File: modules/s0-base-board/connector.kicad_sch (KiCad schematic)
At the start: 6 parts, among them J5 Conn_02x23_Odd_Even, J6 Conn_02x23_Odd_Even, U6 BEAGLEBONEBLACK

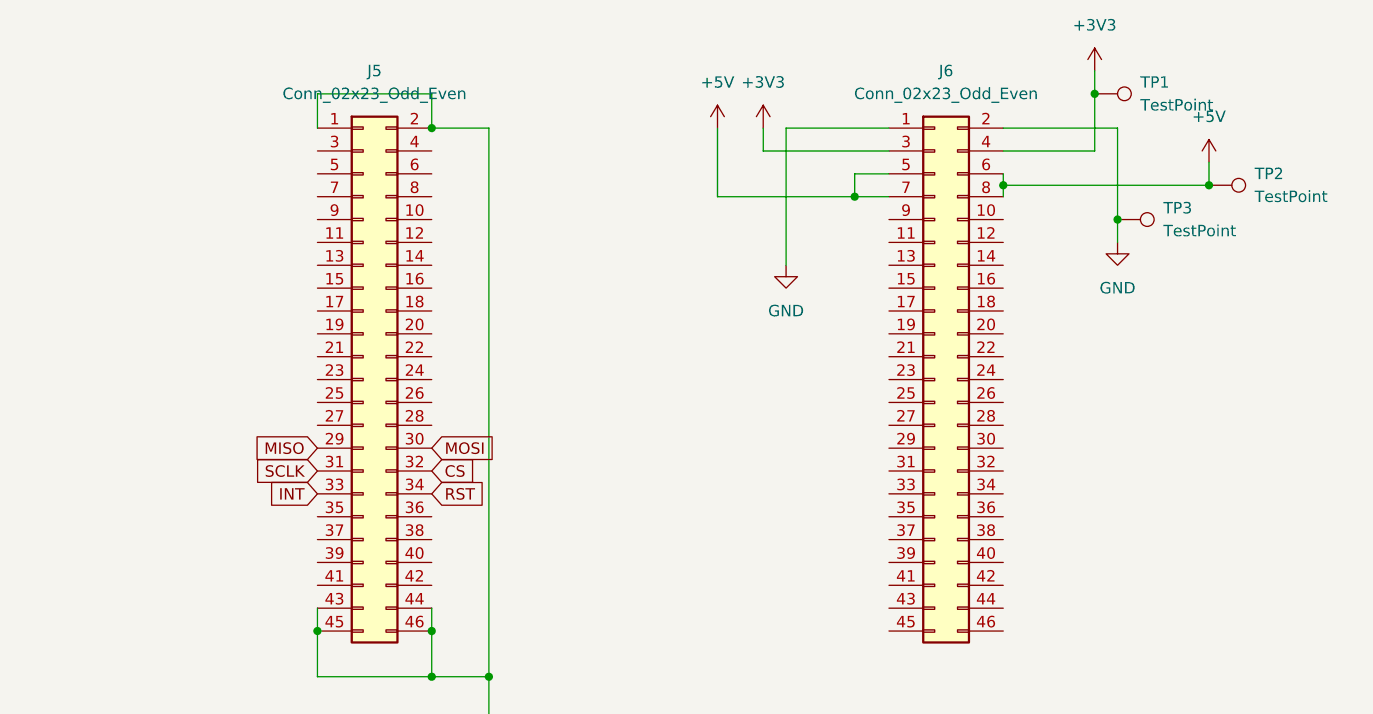
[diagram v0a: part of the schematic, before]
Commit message: feat: add sd card and wired mbus support
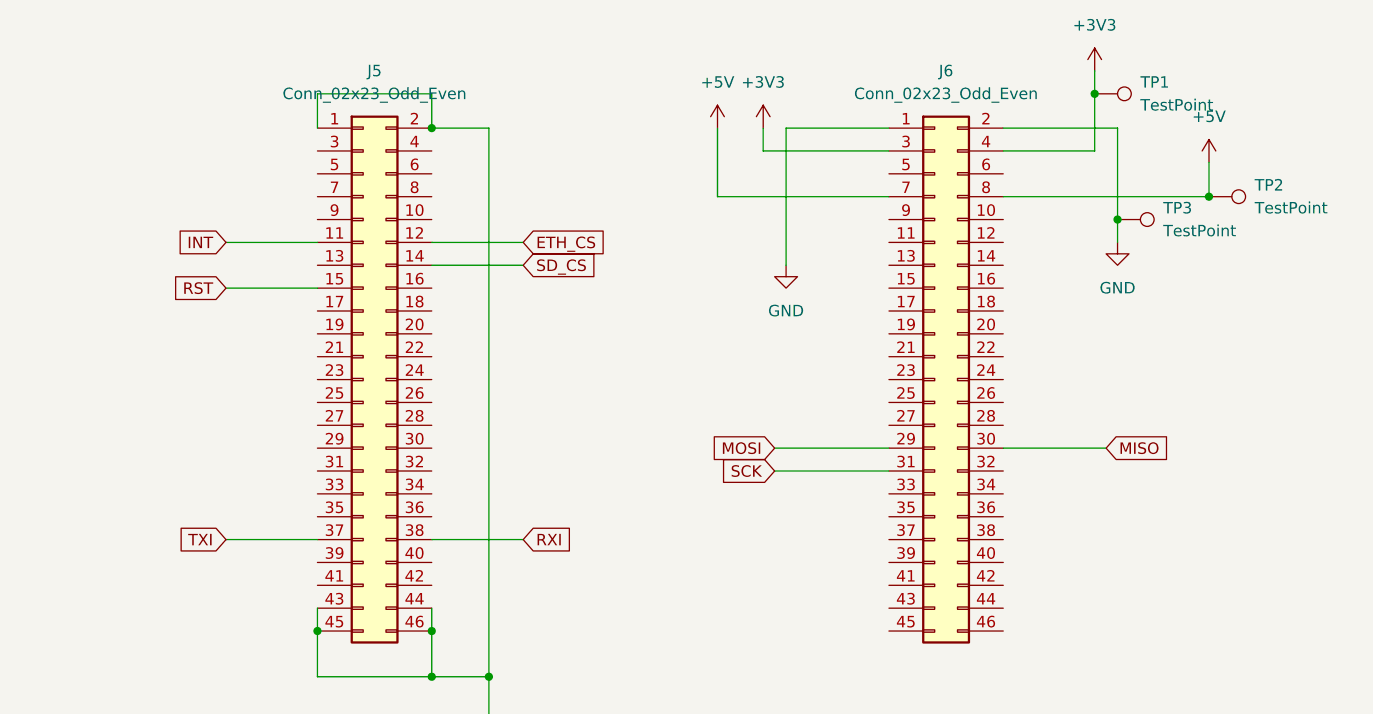
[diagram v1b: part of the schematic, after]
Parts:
- TP1, TP2, TP3, U6: now left out of the parts list
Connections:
- net +5V: no longer J6.5 (Pin_5), J6.6 (Pin_6)
- net INT: now also J5.11 (Pin_11); no longer J5.33 (Pin_33)
- net MISO: now also J6.30 (Pin_30); no longer J5.29 (Pin_29)
- net MOSI: now also J6.29 (Pin_29); no longer J5.30 (Pin_30)
- net RST: now also J5.15 (Pin_15); no longer J5.34 (Pin_34)
- net SCK: now reaches J6.31 (Pin_31)
- net ETH_CS: now reaches J5.12 (Pin_12)
- net SD_CS: now reaches J5.14 (Pin_14)
- net TXI: now reaches J5.37 (Pin_37)
- net RXI: now reaches J5.38 (Pin_38)
- net CS: no longer names the net of J5.32 (Pin_32)
- net SCLK: no longer names the net of J5.31 (Pin_31)
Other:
- moved on the sheet: TP2

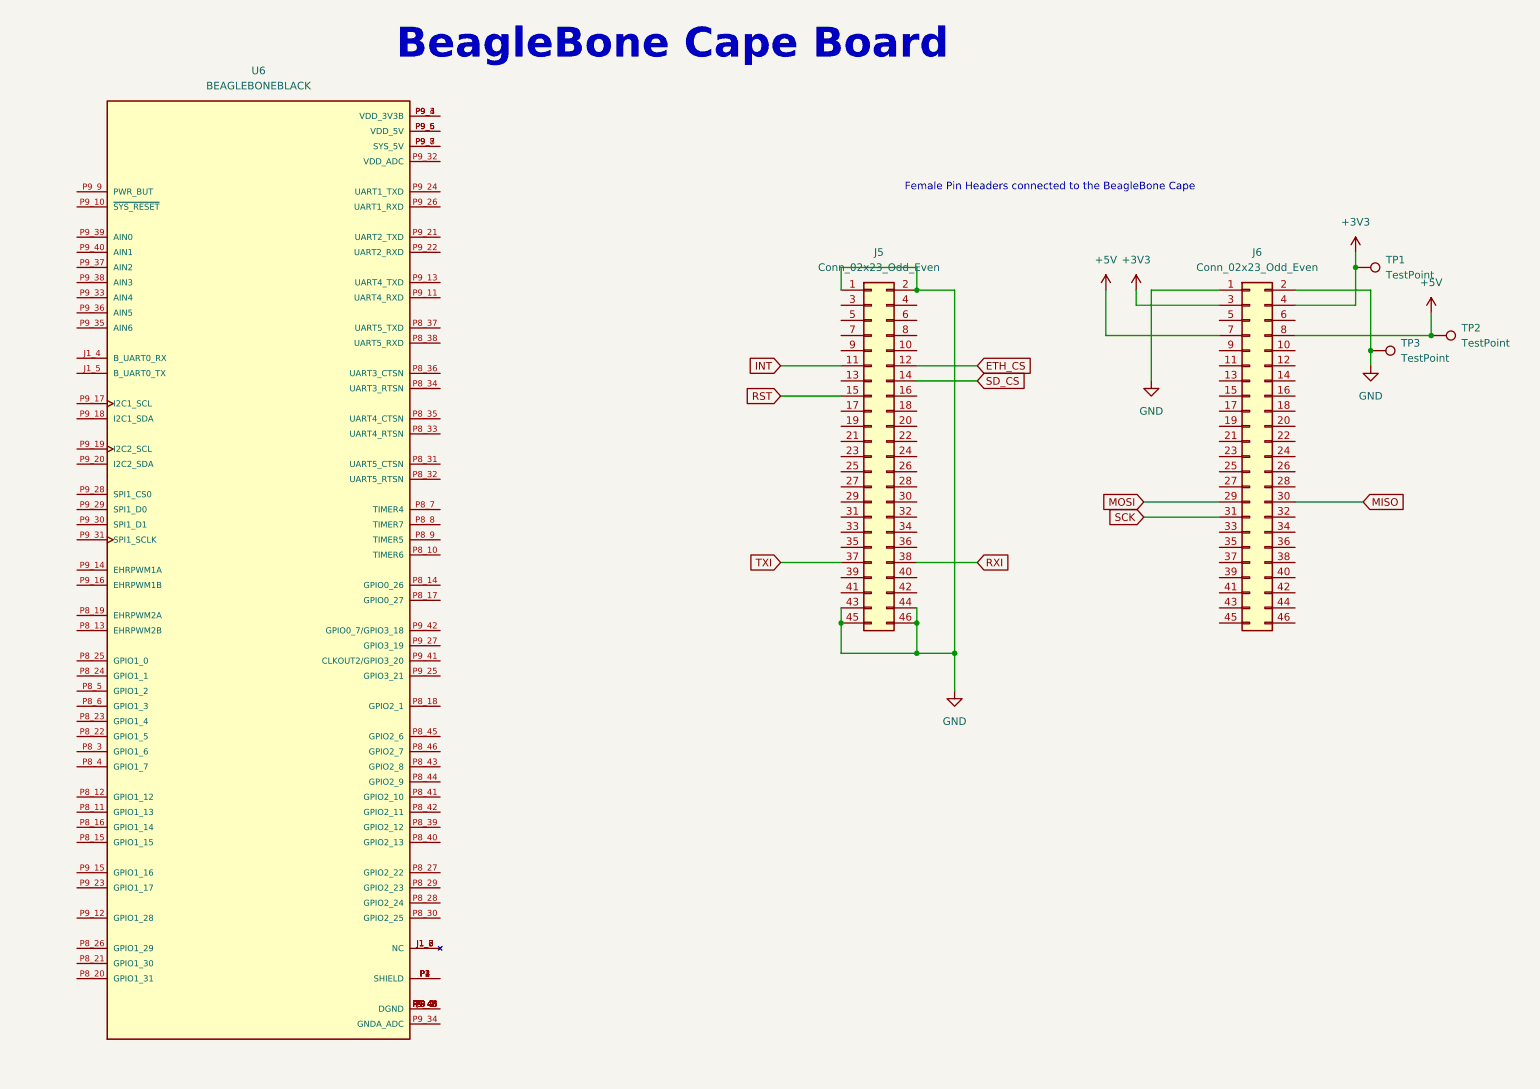
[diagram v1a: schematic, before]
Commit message: feat(base-board): route and add wirembus support
Signed-off-by: Rodney Osodo <socials@rodneyosodo.com>
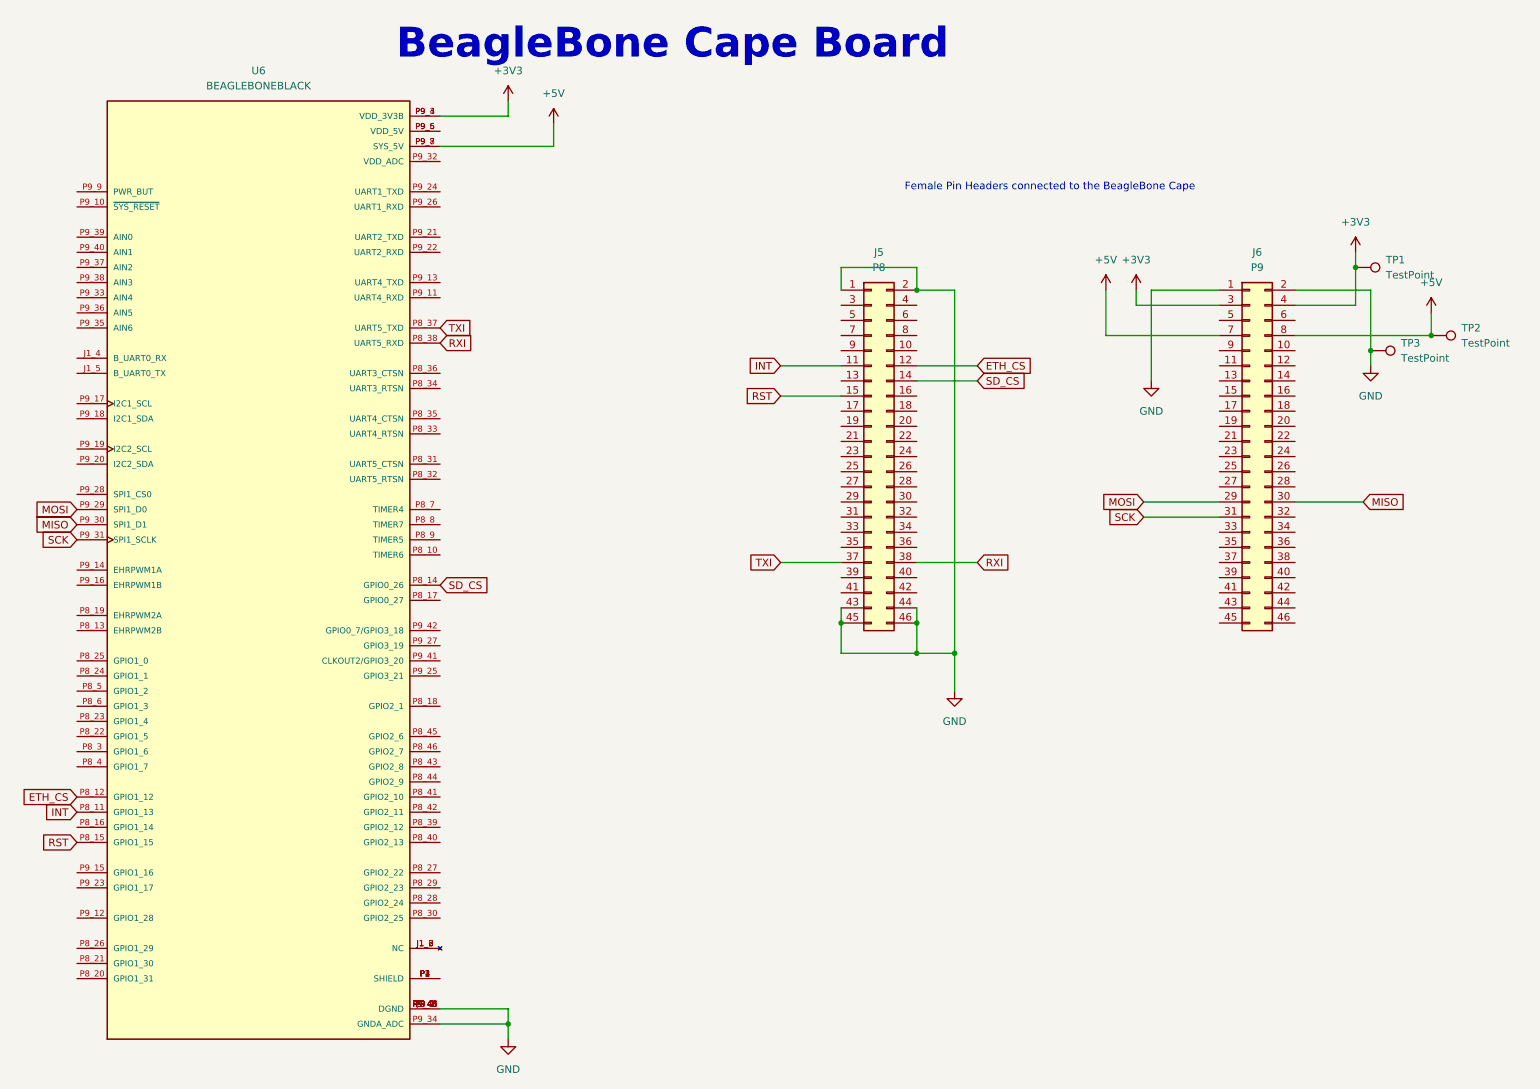
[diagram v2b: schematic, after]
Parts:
- J5: value Conn_02x23_Odd_Even -> P8
- J6: value Conn_02x23_Odd_Even -> P9
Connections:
- net +3V3: now also U6.P9_3 (VDD_3V3B), U6.P9_4 (VDD_3V3B)
- net +5V: now also U6.P9_7 (SYS_5V), U6.P9_8 (SYS_5V)
- net ETH_CS: now also U6.P8_12 (GPIO1_12)
- net GND: now also U6.J1_1 (DGND), U6.P8_1 (DGND), U6.P8_2 (DGND), U6.P9_1 (DGND), U6.P9_2 (DGND), U6.P9_34 (GNDA_ADC), U6.P9_43 (DGND), U6.P9_44 (DGND), U6.P9_45 (DGND), U6.P9_46 (DGND)
- net INT: now also U6.P8_11 (GPIO1_13)
- net MISO: now also U6.P9_30 (SPI1_D1)
- net MOSI: now also U6.P9_29 (SPI1_D0)
- net RST: now also U6.P8_15 (GPIO1_15)
- net RXI: now also U6.P8_38 (UART5_RXD)
- net SCK: now also U6.P9_31 (SPI1_SCLK)
- net SD_CS: now also U6.P8_14 (GPIO0_26)
- net TXI: now also U6.P8_37 (UART5_TXD)

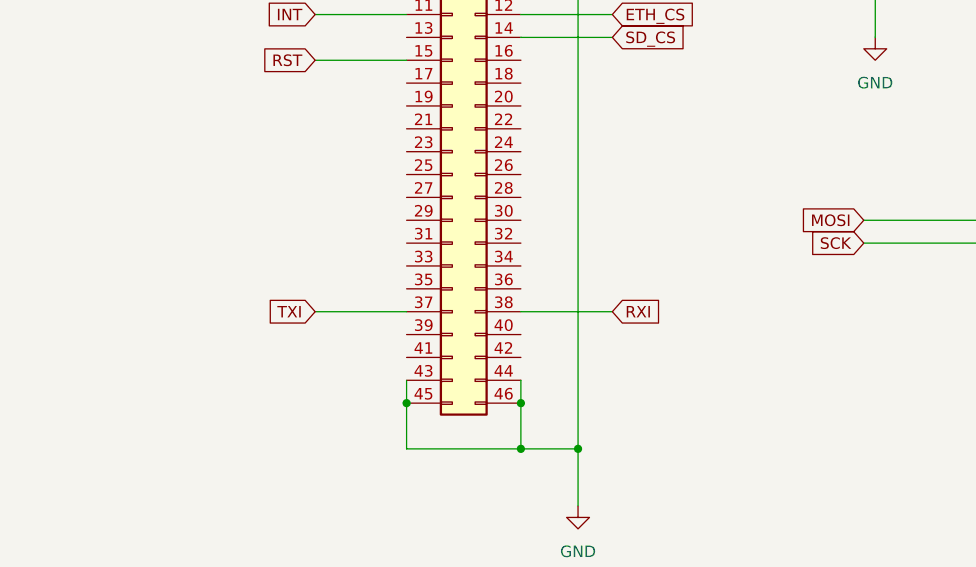
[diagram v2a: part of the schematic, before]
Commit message: feat: add open solder jumper to switch off wired mbus
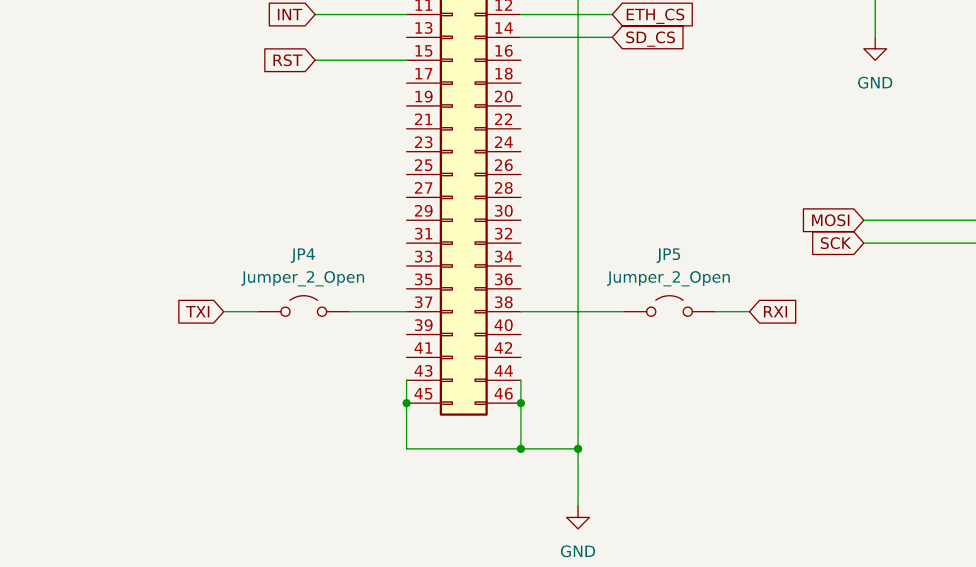
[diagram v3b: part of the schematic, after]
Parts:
- added JP4, JP5: Jumper_2_Open, Jumper:SolderJumper-2_P1.3mm_Open_RoundedPad1.0x1.5mm, symbol Jumper:Jumper_2_Open
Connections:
- net RXI: now also JP5.2 (B); no longer J5.38 (Pin_38)
- net TXI: now also JP4.1 (A); no longer J5.37 (Pin_37)
- new net: J5.37 (Pin_37), JP4.2 (B)
- new net: J5.38 (Pin_38), JP5.1 (A)
